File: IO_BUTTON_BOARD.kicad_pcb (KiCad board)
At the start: 2 copper layers, 80 x 40 mm, 131 parts, among them P1 I2C, P10 IO_7, P2 I2C, P3 IO_0, P4 IO_1, P5 IO_2, P6 IO_3, P7 IO_4, P8 IO_5, P9 IO_6, Q1 NPN, Q10 PNP, Q11 PNP, Q12 PNP, Q13 PNP, Q14 PNP, Q15 PNP, Q16 PNP, Q17 PNP, Q2 PNP, Q3 NPN, Q4 PNP, Q5 NPN, Q6 NPN, Q7 PNP, Q8 PNP, Q9 NPN, SW1 CONFIG, SW2 SW_0, SW3 SW_1, SW4 SW_2, SW5 SW_3, SW6 SW_4, SW7 SW_5, SW8 SW_6, SW9 SW_7, U1 PCF8574A, U2 74HC86, U3 74HC86

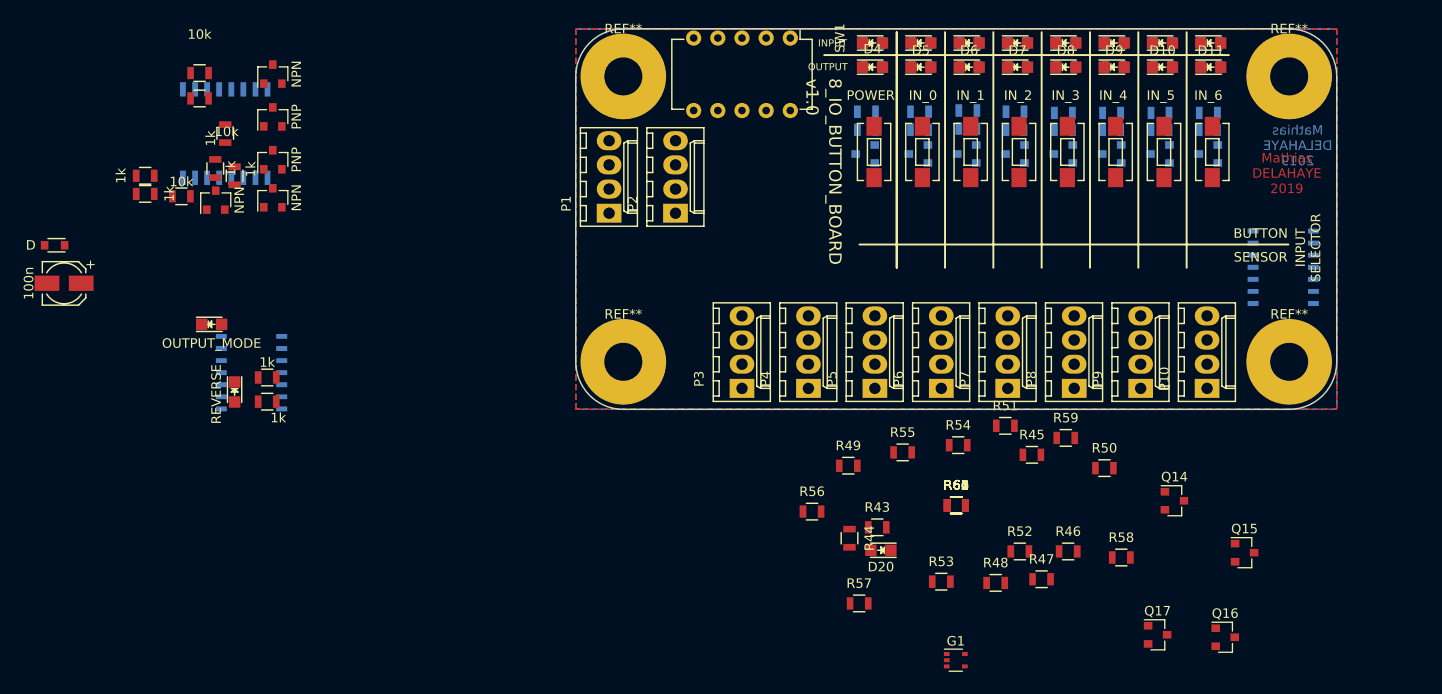
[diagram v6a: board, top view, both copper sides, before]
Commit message: Add manual routing, XOR gates remains to be routed
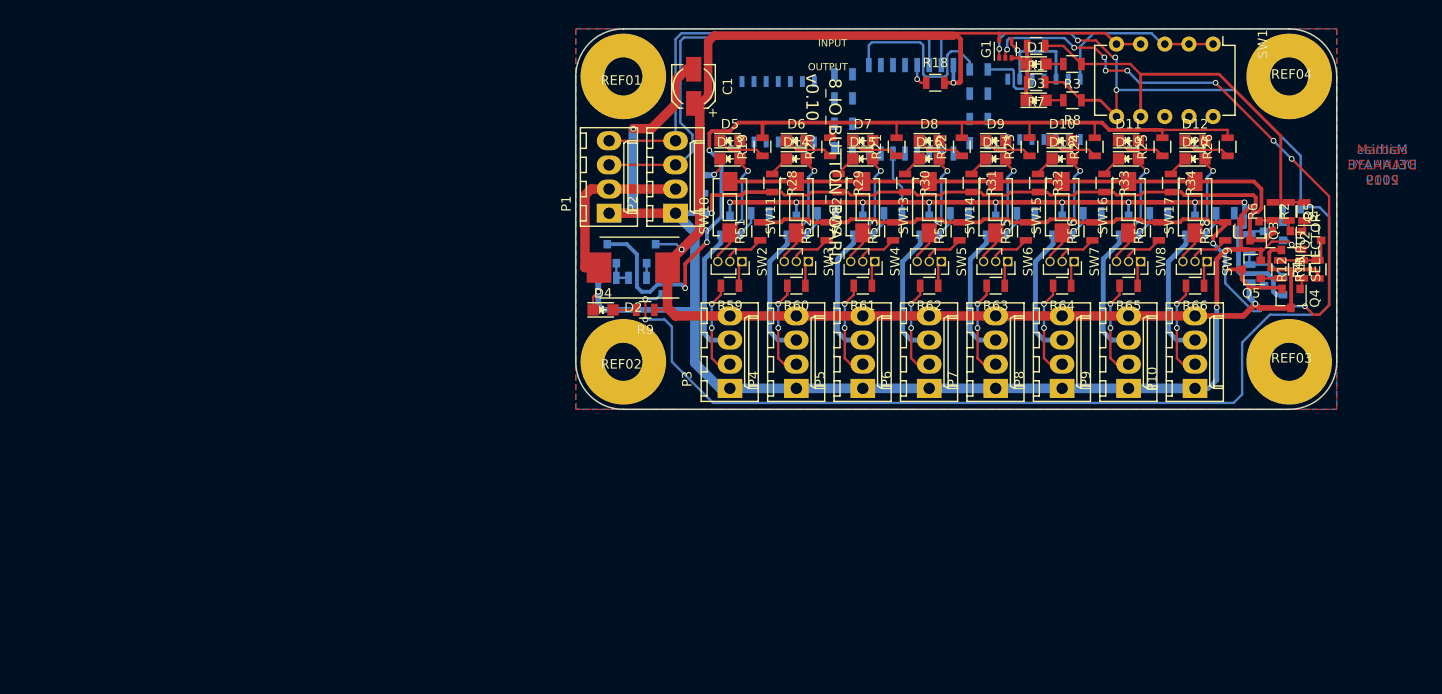
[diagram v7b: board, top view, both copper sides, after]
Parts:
- added SW10: SW_Push, Buttons_Switches_SMD:SW_SPST_EVQPE1, F.Cu at (116.2, 118.7)
- added SW11: SW_Push, Buttons_Switches_SMD:SW_SPST_EVQPE1, F.Cu at (123.2, 118.7)
- added SW12: SW_Push, Buttons_Switches_SMD:SW_SPST_EVQPE1, F.Cu at (130.2, 118.7)
- added SW13: SW_Push, Buttons_Switches_SMD:SW_SPST_EVQPE1, F.Cu at (137.2, 118.7)
- added SW14: SW_Push, Buttons_Switches_SMD:SW_SPST_EVQPE1, F.Cu at (144.1, 118.7)
- added SW15: SW_Push, Buttons_Switches_SMD:SW_SPST_EVQPE1, F.Cu at (151.1, 118.7)
- added SW16: SW_Push, Buttons_Switches_SMD:SW_SPST_EVQPE1, F.Cu at (158.1, 118.7)
- added SW17: SW_Push, Buttons_Switches_SMD:SW_SPST_EVQPE1, F.Cu at (165.1, 118.7)
- D2: footprint Diodes_SMD:D_0805 -> Diodes_SMD:DO-214AB
- Q14, Q15, Q16, Q17, R10, R43, R44, R45, R46, R47, R48, R49, R50: moved to B.Cu
- R12, R13, R18, R19, R20, R21, R22, R23, R24, R25, R26, R28, R29, R30, R31, R32, R33, R34: moved to F.Cu
- SW2, SW3, SW4, SW5, SW6, SW7, SW8, SW9: footprint Buttons_Switches_SMD:SW_SPST_EVQPE1 -> Pin_Header_1.27:PinSocket_1x03_P1.27mm_Vertical
- moved R10 120.6 mm to (175.3, 118.7)
- moved R2 118.1 mm to (176.6, 119.2), turned to 90 degrees
- moved R4 115.7 mm to (178.0, 125.3), turned to 90 degrees
- moved Q1 115.3 mm to (177.4, 122.2), turned to 0 degrees
- moved R5 115.1 mm to (174.9, 119.2), turned to 270 degrees
- moved R6 113.8 mm to (173.3, 119.2), turned to 90 degrees
- moved Q4 108.7 mm to (175.2, 128.3), turned to 270 degrees
- moved Q2 106.4 mm to (174.2, 122.2), turned to 270 degrees
- moved Q5 104.9 mm to (171.0, 125.3), turned to 180 degrees
- moved Q3 102.8 mm to (170.9, 121.2), turned to 270 degrees
- moved R7 94.4 mm to (148.4, 105.6), turned to 180 degrees
- moved R3 91.8 mm to (152.2, 103.7)
- moved D1 91.0 mm to (148.4, 103.7), turned to 0 degrees
- moved D3 89.8 mm to (148.4, 107.5)
- moved R8 88.4 mm to (152.2, 107.5), turned to 180 degrees
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- renumbered REF** to REF01, REF** to REF02, REF** to REF03, REF** to REF04
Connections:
- P10 pad 2: (no net) -> /IN_7
- P3 pad 2: (no net) -> /IN_0
- P4 pad 2: (no net) -> /IN_1
- P5 pad 2: (no net) -> /IN_2
- P6 pad 2: (no net) -> /IN_3
- P7 pad 2: (no net) -> /IN_4
- P8 pad 2: (no net) -> /IN_5
- P9 pad 2: (no net) -> /IN_6
- R59 pad 2: (no net) -> /IN_0
- R60 pad 2: (no net) -> /IN_1
- R61 pad 2: (no net) -> /IN_2
- R62 pad 2: (no net) -> /IN_3
- R63 pad 2: (no net) -> /IN_4
- R64 pad 2: (no net) -> /IN_5
- R65 pad 2: (no net) -> /IN_6
- R66 pad 2: (no net) -> /IN_7
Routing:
- net GND: track 0.00 -> 244.5 mm, vias 0 -> 5
- net VCC: track 0.00 -> 174.7 mm, vias 0 -> 3
- net /ACTIVE_OUTPUT: track 0.00 -> 160.6 mm, vias 0 -> 6
- net /PULL_LANE: track 0.00 -> 133.7 mm, vias 0 -> 11
- net /INPUT_LED_GND: track 0.00 -> 98.1 mm, vias 0 -> 3
- net /OUTPUT_VCC: track 0.00 -> 79.7 mm, vias 0 -> 9
- net /CONTACT_LANE: track 0.00 -> 65.3 mm
- net /SCL: track 0.00 -> 50.5 mm
- net /SDA: track 0.00 -> 49.0 mm
- net /REVERSE_PULL: track 0.00 -> 43.4 mm
- net /OUT_1: track 0.00 -> 24.4 mm, vias 0 -> 1
- net /OUT_0: track 0.00 -> 24.2 mm, vias 0 -> 1
- net /OUT_7: track 0.00 -> 24.0 mm, vias 0 -> 1
- net /OUT_5: track 0.00 -> 24.0 mm, vias 0 -> 1
- net /OUT_3: track 0.00 -> 24.0 mm, vias 0 -> 1
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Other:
- net class Default: clearance 0.2 -> 0.1524
- net class medium_current added: clearance 0.2, trace_width 0.4, via_dia 0.6, via_drill 0.4
- rule trace_clearance: 0.2 -> 0.1524
- board text added: "v0.10"
- board text removed: "BUTTON"
- board text removed: "SENSOR"
- board text removed: "v1.0"

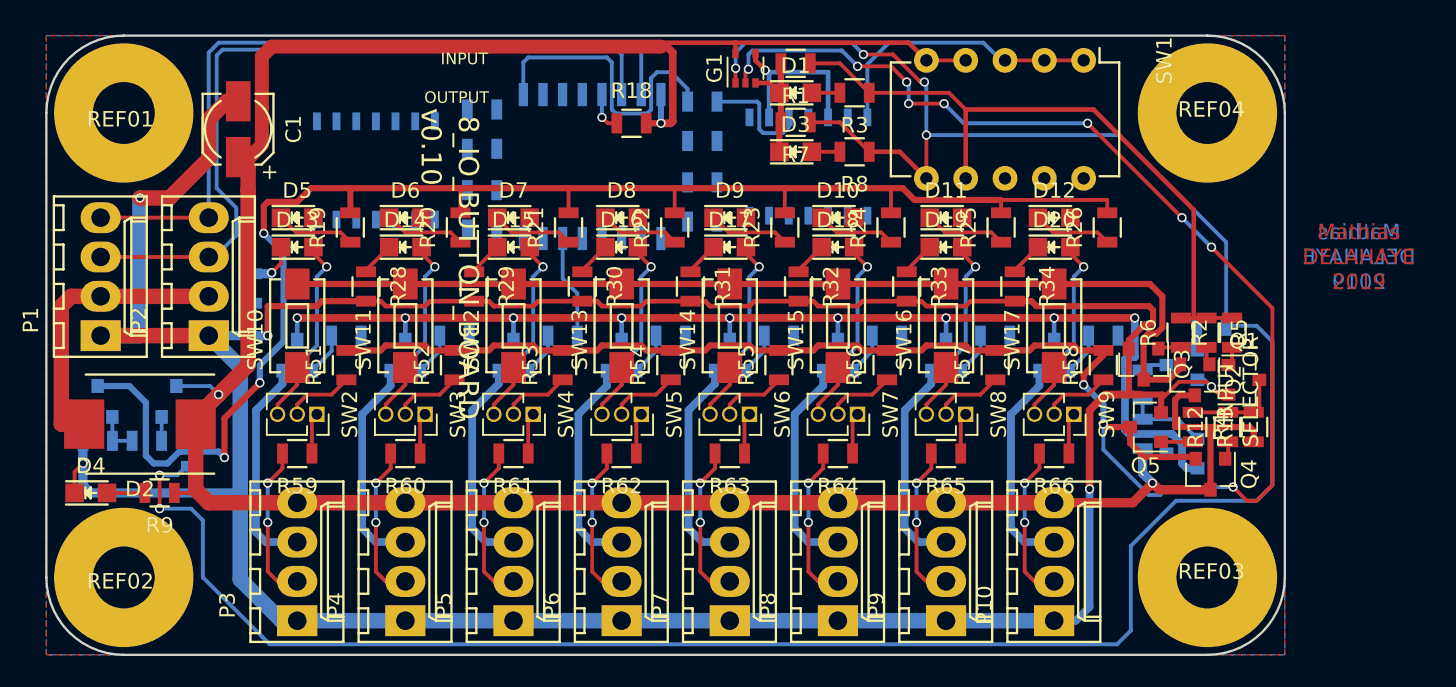
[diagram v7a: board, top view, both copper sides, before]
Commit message: Add routing, logical tracks remains to be added
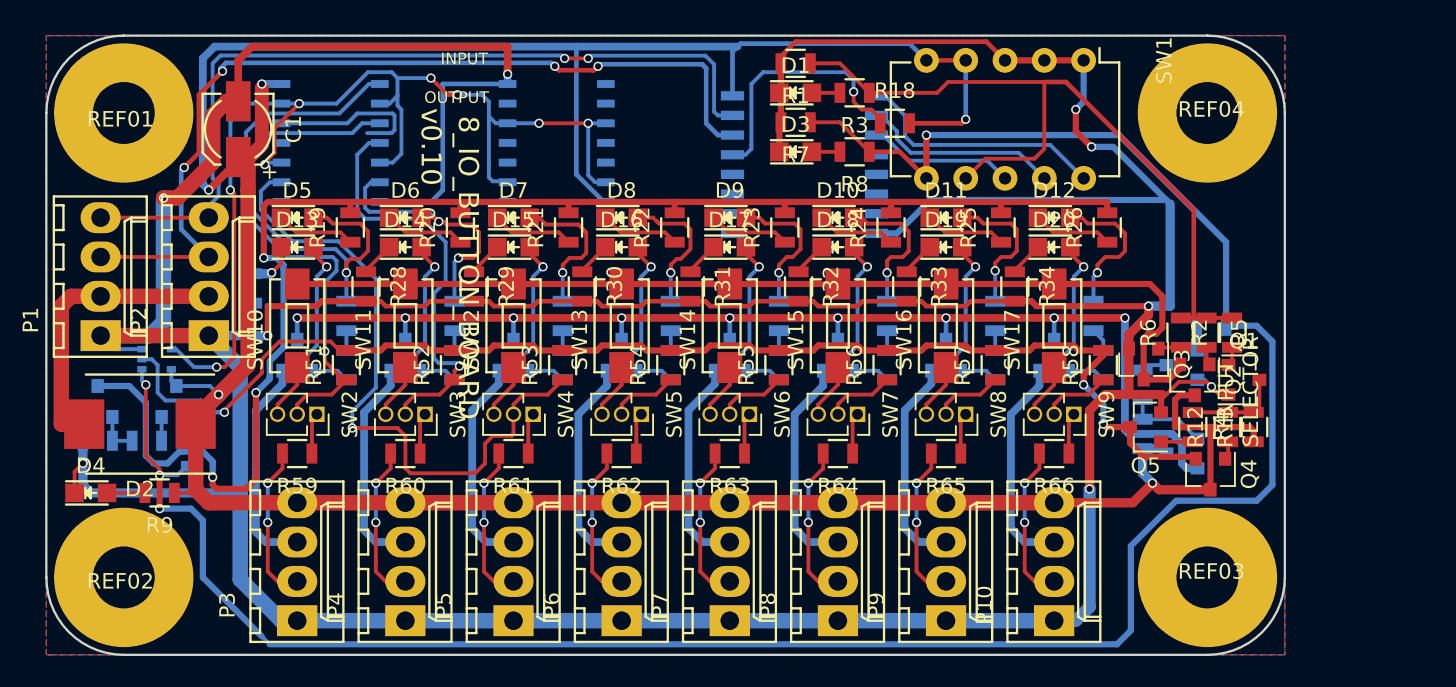
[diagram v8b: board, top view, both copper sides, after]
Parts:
- G1: moved to B.Cu
- moved G1 42.4 mm to (107.1, 120.9), turned to 0 degrees
- moved R35 26.0 mm to (167.6, 118.1), turned to 90 degrees
- moved R36 22.0 mm to (161.3, 118.1), turned to 90 degrees
- moved R39 18.1 mm to (140.3, 118.1), turned to 90 degrees
- moved R18 17.0 mm to (154.8, 105.7)
- moved U3 16.2 mm to (133.1, 106.9), turned to 90 degrees
- moved R37 14.7 mm to (154.3, 118.1), turned to 90 degrees
- moved R38 14.7 mm to (147.3, 118.1), turned to 90 degrees
- moved U1 13.7 mm to (149.0, 108.3), turned to 180 degrees
- moved R40 12.0 mm to (133.3, 118.1), turned to 90 degrees
- moved R42 12.0 mm to (119.4, 118.1), turned to 90 degrees
- moved R41 5.86 mm to (126.4, 118.1), turned to 90 degrees
- moved U2 3.47 mm to (118.2, 106.9), turned to 270 degrees
- moved R43 1.91 mm to (119.4, 121.3), turned to 90 degrees
- moved R44 1.91 mm to (126.4, 121.3), turned to 90 degrees
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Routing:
- net GND: track 244.5 -> 326.2 mm, vias 5 -> 9
- net /REF_XOR: track 11.3 -> 71.6 mm, vias 1 -> 8
- net /PULL_LANE: track 133.7 -> 84.2 mm, vias 11 -> 3
- net Net-(R53-Pad1): track 4.47 -> 42.7 mm, vias 0 -> 1
- net Net-(R51-Pad1): track 4.47 -> 35.5 mm, vias 0 -> 1
- net Net-(D5-Pad2): track 0.00 -> 30.9 mm, vias 0 -> 1
- net VCC: track 174.7 -> 204.0 mm, vias 3 -> 5
- net Net-(R52-Pad1): track 4.47 -> 27.6 mm, vias 0 -> 1
- net Net-(R38-Pad1): track 19.7 -> 1.48 mm
- net Net-(D6-Pad2): track 0.00 -> 17.3 mm, vias 0 -> 2
- net Net-(SW1-Pad10): track 0.00 -> 16.4 mm
- net Net-(R18-Pad1): track 2.59 -> 16.6 mm
- net Net-(SW1-Pad9): track 0.00 -> 12.8 mm
- net /ACTIVE_OUTPUT: track 160.6 -> 149.0 mm, vias 6 -> 4
- net Net-(R54-Pad1): track 4.47 -> 14.9 mm
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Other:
- board text removed: "Mathias DELAHAYE 2019"
